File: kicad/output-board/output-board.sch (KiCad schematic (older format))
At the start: 15 parts, among them P1 CONN_2, P2 CONN_5, SW1 SW_PUSH_SMALL, U1 PANSTAMP_02, U2 UA78M33

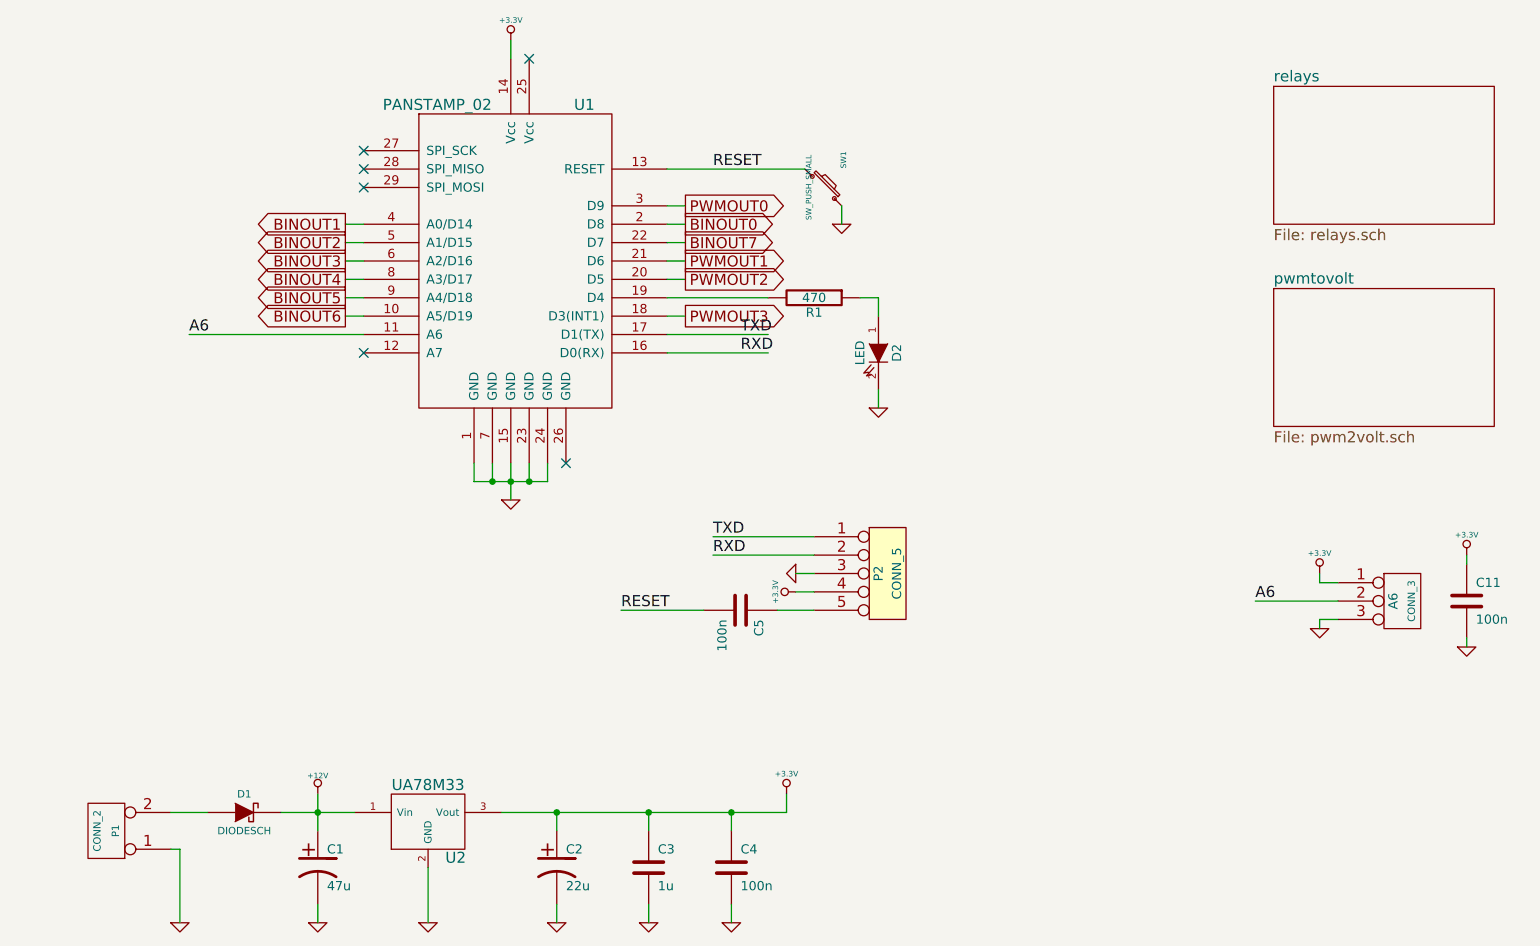
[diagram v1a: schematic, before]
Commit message: Buffer removed in pwm2volt circuit
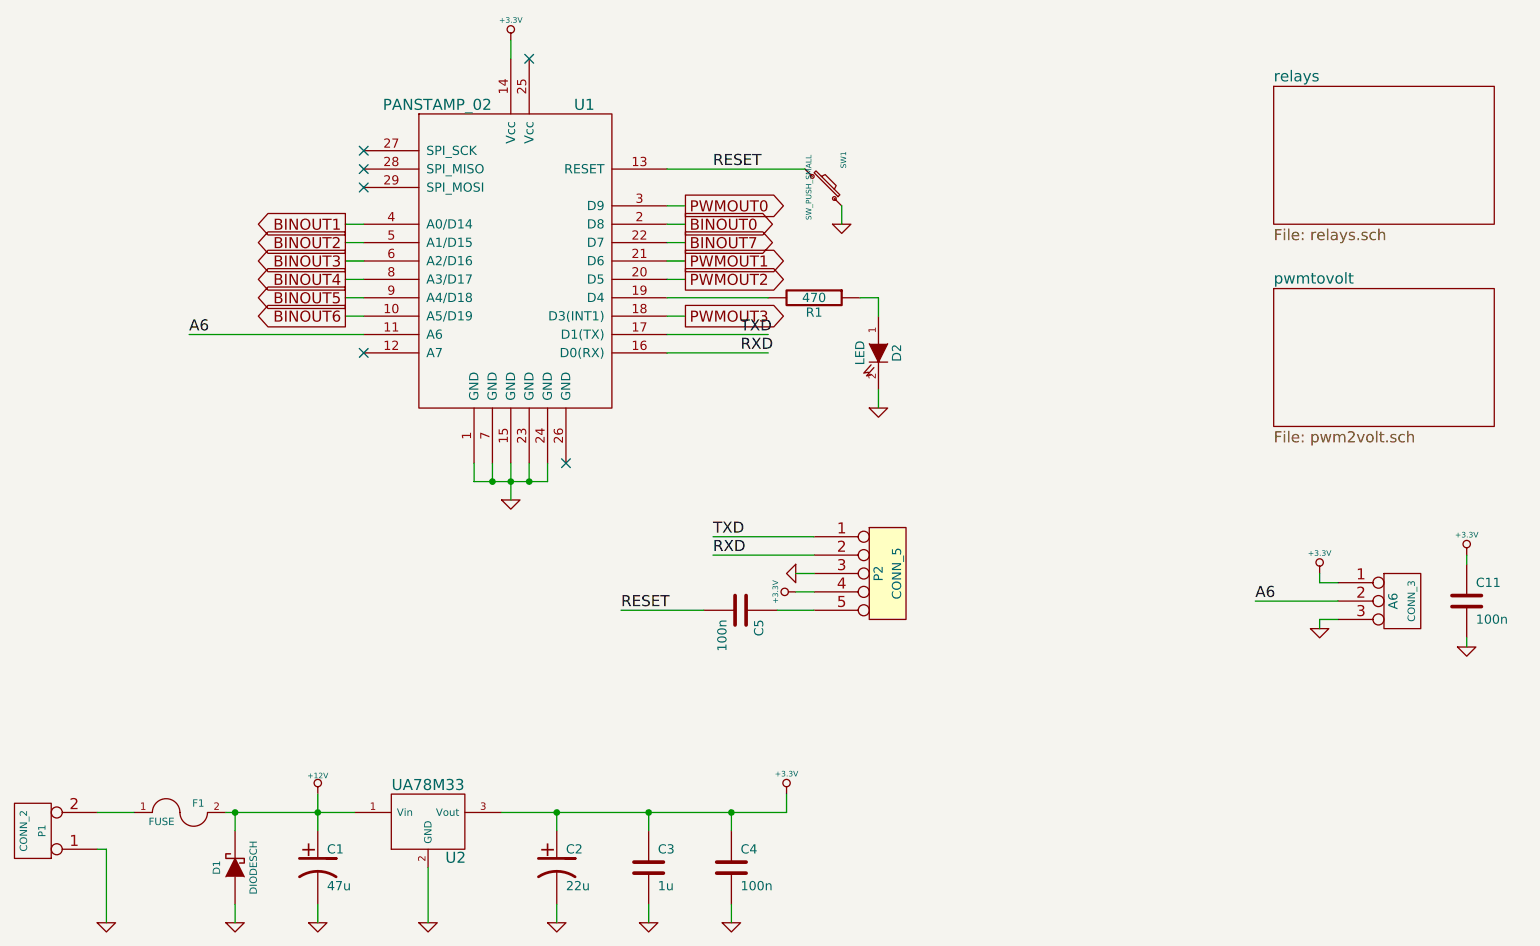
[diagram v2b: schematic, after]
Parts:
- added F1: FUSE, SM1206, symbol FUSE
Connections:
- net +12V: now also F1.2
- net GND: now also D1.1 (A)
- net at P1.2 (PM): now also F1.1; no longer D1.1 (A)
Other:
- moved on the sheet: D1, P1

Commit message: New PCB layout in accordance with the CE directives
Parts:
- P3: renamed from A6; value CONN_3 -> CONN_4; footprint SIL-3 -> SIL-4; symbol CONN_3 -> CONN_4
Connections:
- net +3.3V: now also P3.4 (P4); no longer P3.1 (P1)
- net GPIO1: now reaches U1.12 (A7)
- net GPIO1: now also P3.2 (P2)
- net A6 renamed GPIO0
- net GPIO0: now also P3.1 (P1); no longer P3.2 (PM)
- no-connect marks 6 -> 5
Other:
- moved on the sheet: C11
